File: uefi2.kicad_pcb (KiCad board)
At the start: 4 copper layers, 115.1 x 100 mm, 143 parts, among them J10 Conn_02x08_Odd_Even, J2 Conn_02x10_Odd_Even, J3 Conn_02x03_Odd_Even, J4 Conn_02x04_Odd_Even, J5 Conn_02x09_Odd_Even, J6 Conn_01x06, J7 Conn_01x05_Male, J8 USB_B_Mini, J9 USB_C, M1 Module-power_12and5V-0.2, M2 Module-knock-0.2, M3 Module-vr-discrete-0.5, M4 Module-vr-max9924-0.1, M5 Module-wbo-0.5, M6 Module:mega-mcu100/0.3, M7 Module-can-0.1, P1 Pad, P15 Pad, P16 Pad, P17 Pad, P18 Pad, P2 Pad, P3 Pad, P4 Pad, P7 Pad, P8 Pad, Q10 ISL9V3040D3ST, Q11 ISL9V3040D3ST, Q12 ISL9V3040D3ST, Q7 ISL9V3040D3ST, Q8 ISL9V3040D3ST, Q9 ISL9V3040D3ST, U1 TLE9201SG, U10 VNLD5160TR-E, U11 VNLD5160TR-E, U2 TLE9201SG, U3 MPX4/MPXH6400_MAP, U4 MAX31855KASA, U5 JDY-33, U6 VNLD5160TR-E, U7 VNLD5160TR-E, U8 VNLD5160TR-E, U9 VNLD5160TR-E

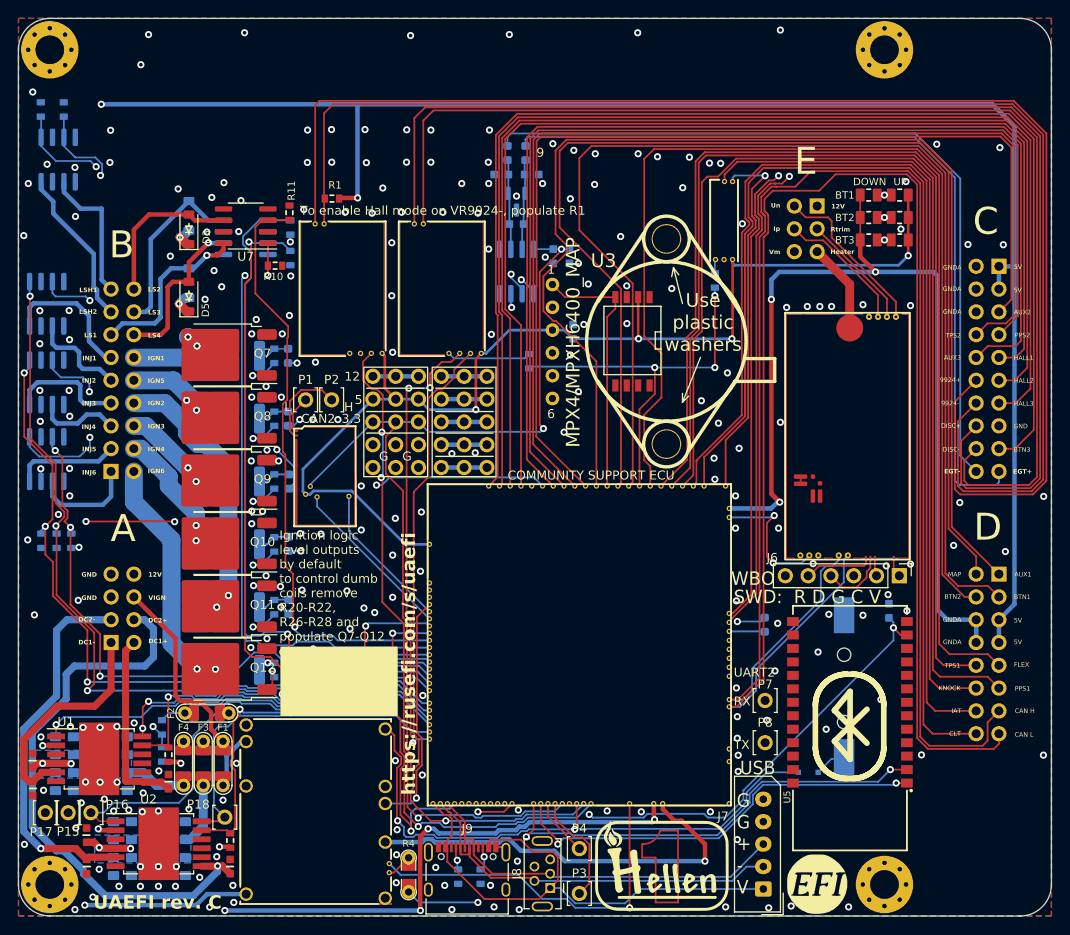
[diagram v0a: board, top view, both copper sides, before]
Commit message: change revision from a to A0, change kicad file
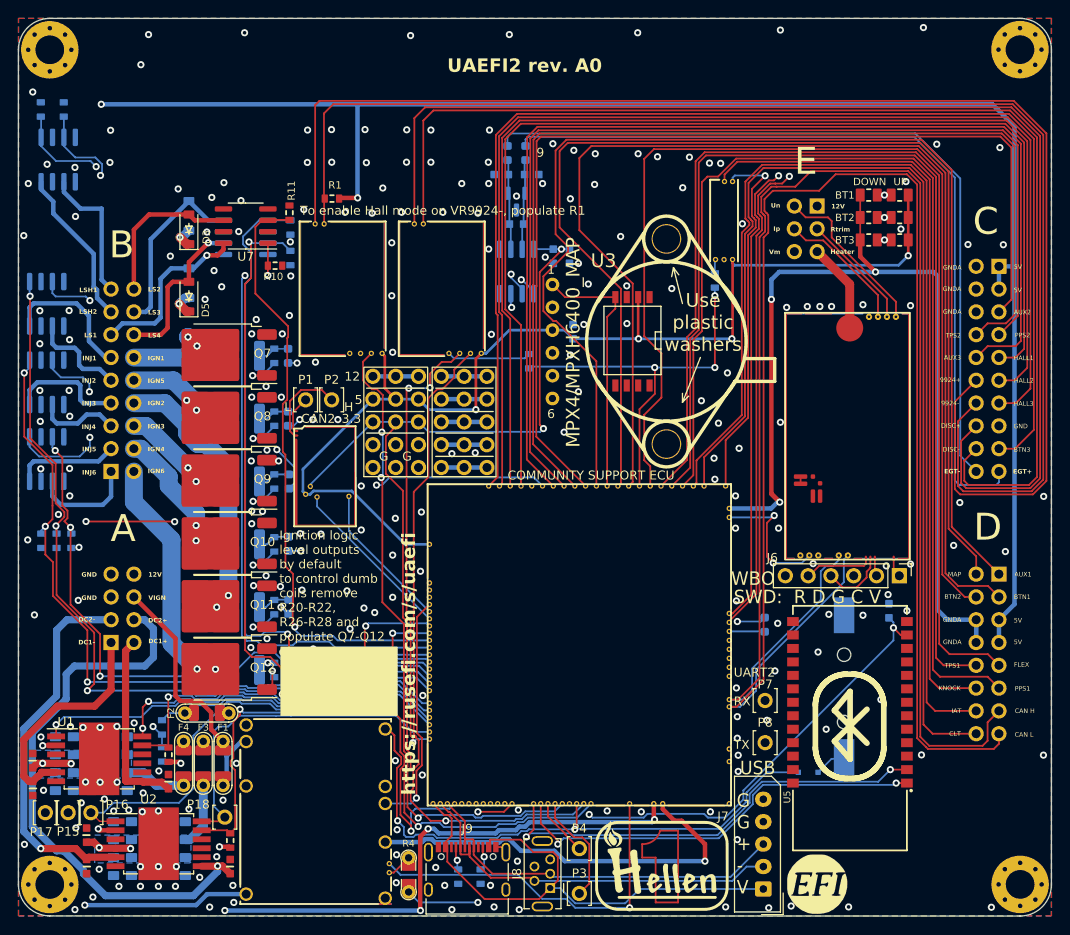
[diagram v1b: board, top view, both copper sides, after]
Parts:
- removed H3, H4: M3, MountingHole:MountingHole_3.2mm_M3_Pad_Via
- added H1: M3, MountingHole:MountingHole_3.2mm_M3_Pad_Via, F.Cu at (161.6, 63.5)
- added H1: M3, MountingHole:MountingHole_3.2mm_M3_Pad_Via, F.Cu at (161.6, 156.5)
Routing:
- net GND: vias 243 -> 245
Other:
- board text added: "UAEFI2 rev. A0"
- board text removed: "UAEFI rev. C"
